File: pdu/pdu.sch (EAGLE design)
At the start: 62 parts, among them IC1 FDN359BN, IC2 FDN359BN, IC3 FDN359BN, J1 S2B-PH-K-S(LF)(SN), J10 S2B-PH-K-S(LF)(SN), J2 S2B-PH-K-S(LF)(SN), J3 S2B-PH-K-S(LF)(SN), J4 S2B-PH-K-S(LF)(SN), J5 S2B-PH-K-S(LF)(SN), J6 S2B-PH-K-S(LF)(SN), J7 S2B-PH-K-S(LF)(SN), J8 S2B-PH-K-S(LF)(SN), J9 S2B-PH-K-S(LF)(SN)

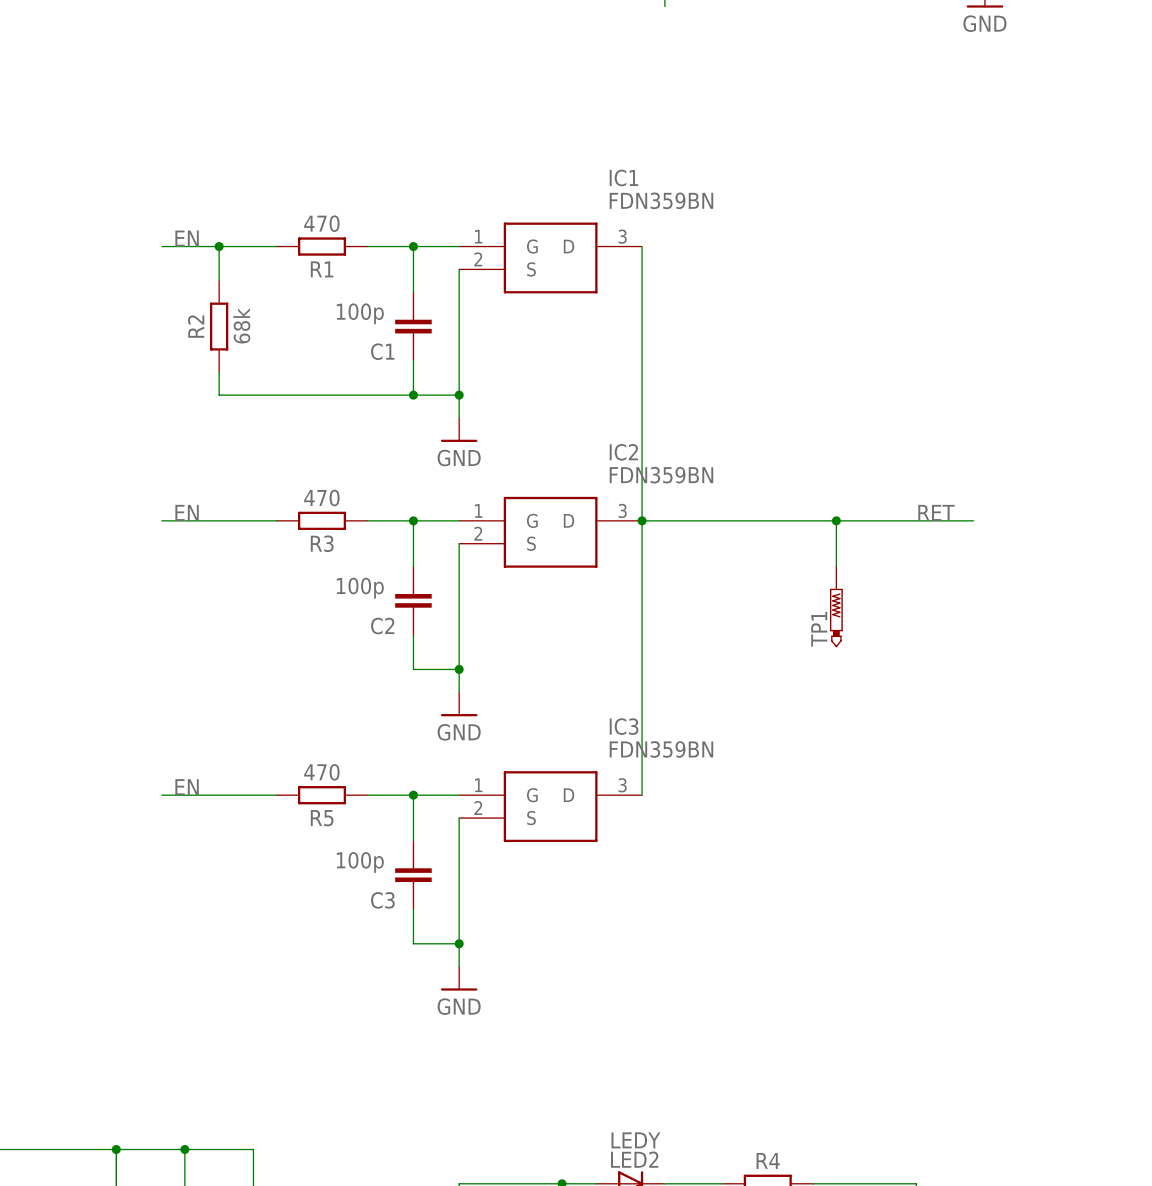
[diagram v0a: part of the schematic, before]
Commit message: change to single big fet
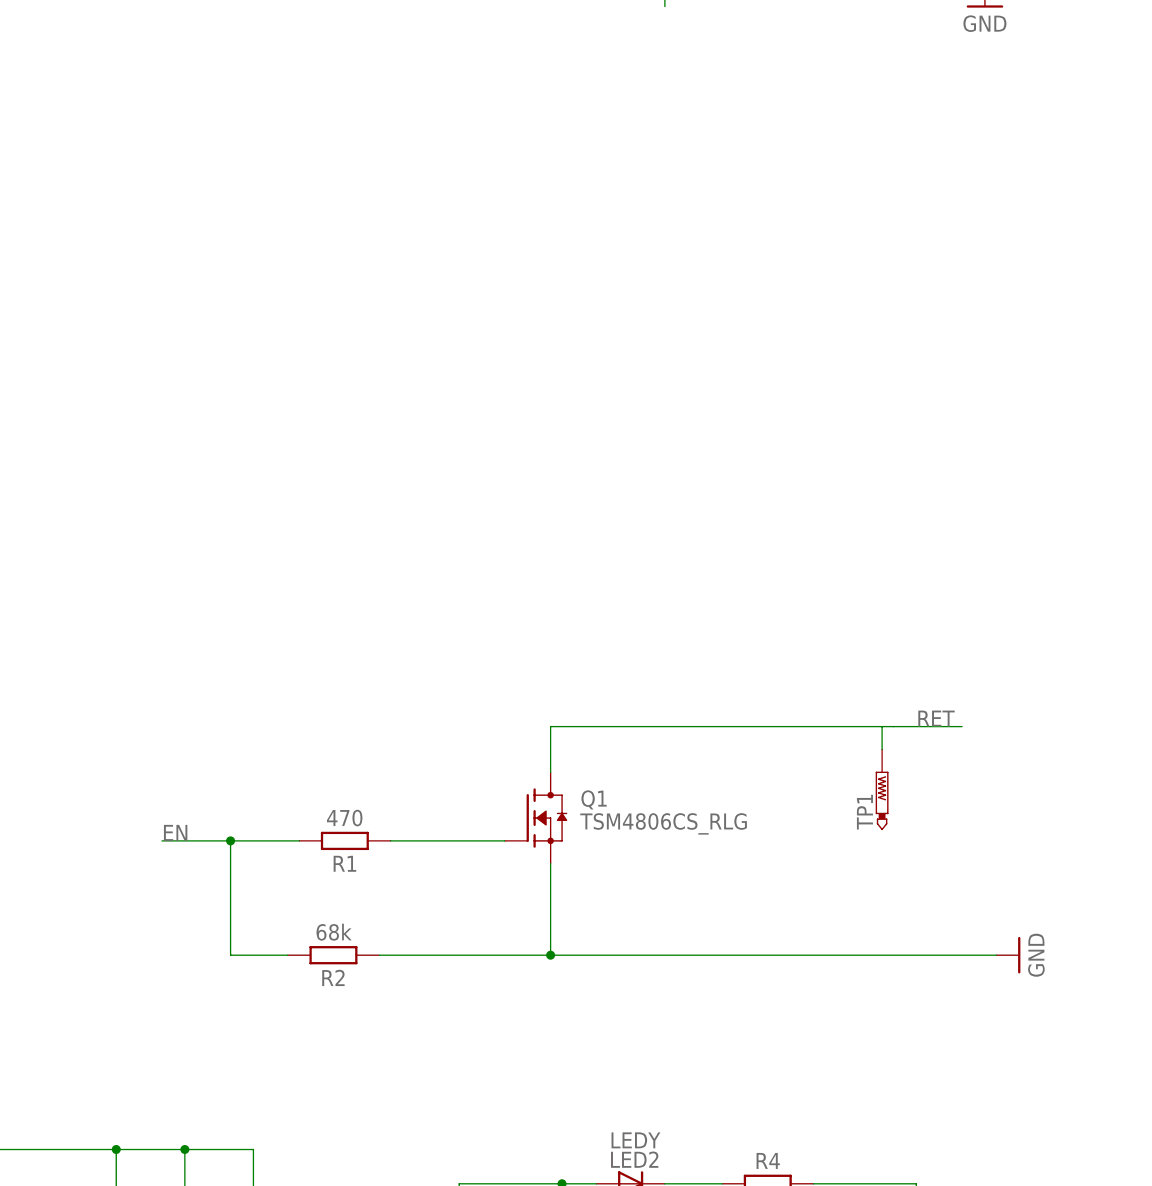
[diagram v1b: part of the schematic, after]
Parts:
- removed C1, C2, C3: 100p, Capacitor:C_CHIP-0603(1608-METRIC)
- removed IC1, IC2, IC3: FDN359BN, SamacSys_Parts:FDN359BN
- removed R3, R5: 470, Resistor:R_CHIP-0603(1608-METRIC)
- added Q1: TSM4806CS_RLG, TSM4806CS_RLG:TSM4806CS_RLG
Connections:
- removed net N$2: C2.2, IC2.G, R3.1
- removed net N$3: C3.2, IC3.G, R5.1
- net EN: no longer R3.2, R5.2
- net GND: now also Q1.S; no longer C1.1, C2.1, C3.1, IC1.S, IC2.S, IC3.S
- net N$1: now also Q1.G; no longer C1.2, IC1.G
- net RET: now also Q1.D; no longer IC1.D, IC2.D, IC3.D
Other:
- moved on the sheet: R1, R2, TP1
